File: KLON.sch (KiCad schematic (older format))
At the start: 37 parts

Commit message: organization. Fixed Values. Stage 1 is complete.
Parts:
- C?: value 3.2n -> 2.2n
- RV?: value POT -> GAIN2
- RV?: value POT -> GAIN1
- gave numbers to parts that had none: 1
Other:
- moved on the sheet: C?, D?, R?, RV?

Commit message: Fixed two connections.
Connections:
- net VB+: now also RV?.2
- net at C?.1, R?.1, R?.2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: now also C?.2
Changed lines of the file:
@@
 LIBS:contrib
 LIBS:valves
-LIBS:dk_USB-DVI-HDMI-Connectors
-LIBS:dk_TVS-Mixed-Technology
-LIBS:dk_TVS-Diodes
-LIBS:dk_Trimmer-Potentiometers
-LIBS:dk_Transistors-JFETs
-LIBS:dk_Transistors-FETs-MOSFETs-Single
-LIBS:dk_Transistors-FETs-MOSFETs-RF
-LIBS:dk_Transistors-FETs-MOSFETs-Arrays
-LIBS:dk_Transistors-Bipolar-BJT-Single
-LIBS:dk_Transistors-Bipolar-BJT-Single-Pre-Biased
-LIBS:dk_Transistors-Bipolar-BJT-RF
-LIBS:dk_Transistors-Bipolar-BJT-Arrays
-LIBS:dk_Toggle-Switches
-LIBS:dk_Thyristors-TRIACs
-LIBS:dk_Thyristors-SCRs
-LIBS:dk_Thyristors-DIACs-SIDACs
-LIBS:dk_Thermal-Cutoffs-Thermal-Fuses
-LIBS:dk_Temperature-Sensors-Analog-and-Digital-Output
-LIBS:dk_Tactile-Switches
-LIBS:dk_Surge-Suppression-ICs
-LIBS:dk_Specialized-Sensors
-LIBS:dk_Specialized-ICs
-LIBS:dk_Solid-State-Relays
-LIBS:dk_Slide-Switches
-LIBS:dk_Signal-Relays-Up-to-2-Amps
-LIBS:dk_Sensors-Transducers_Accessories
-LIBS:dk_Rotary-Potentiometers-Rheostats
-LIBS:dk_RFID-RF-Access-Monitoring-ICs
-LIBS:dk_RF-Transmitters
-LIBS:dk_RF-Transceiver-Modules
-LIBS:dk_RF-Transceiver-ICs
-LIBS:dk_RF-Switches
-LIBS:dk_RF-Receivers
-LIBS:dk_RF-Evaluation-and-Development-Kits-Boards
-LIBS:dk_RF-Detectors
-LIBS:dk_RF-Demodulators
-LIBS:dk_RF-Antennas
-LIBS:dk_RF-Amplifiers
-LIBS:dk_Resistor-Networks-Arrays
-LIBS:dk_Reed-Relays
-LIBS:dk_Rectangular-Connectors-Headers-Male-Pins
-LIBS:dk_Pushbutton-Switches
-LIBS:dk_Programmable-Oscillators
-LIBS:dk_Pressure-Sensors-Transducers
-LIBS:dk_Power-Relays-Over-2-Amps
-LIBS:dk_PMIC-Voltage-Regulators-Special-Purpose
-LIBS:dk_PMIC-Voltage-Regulators-Linear
-LIBS:dk_PMIC-Voltage-Regulators-DC-DC-Switching-Regulators
-LIBS:dk_PMIC-Voltage-Regulators-DC-DC-Switching-Controllers
-LIBS:dk_PMIC-Voltage-Reference
-LIBS:dk_PMIC-V-F-and-F-V-Converters
-LIBS:dk_PMIC-Thermal-Management
-LIBS:dk_PMIC-Supervisors
-LIBS:dk_PMIC-RMS-to-DC-Converters
-LIBS:dk_PMIC-Power-Management-Specialized
-LIBS:dk_PMIC-Power-Distribution-Switches-Load-Drivers
-LIBS:dk_PMIC-OR-Controllers-Ideal-Diodes
-LIBS:dk_PMIC-Motor-Drivers-Controllers
-LIBS:dk_PMIC-LED-Drivers
-LIBS:dk_PMIC-Gate-Drivers
-LIBS:dk_PMIC-Full-Half-Bridge-Drivers
-LIBS:dk_PMIC-Current-Regulation-Management
-LIBS:dk_PMIC-Battery-Management
-LIBS:dk_PMIC-Battery-Chargers
-LIBS:dk_PMIC-AC-DC-Converters-Offline-Switchers
-LIBS:dk_Oscillators
-LIBS:dk_Optoisolators-Triac-SCR-Output
-LIBS:dk_Optoisolators-Transistor-Photovoltaic-Output
-LIBS:dk_Optoisolators-Logic-Output
-LIBS:dk_Optical-Sensors-Reflective-Analog-Output
-LIBS:dk_Optical-Sensors-Phototransistors
-LIBS:dk_Optical-Sensors-Photodiodes
-LIBS:dk_Optical-Sensors-Photo-Detectors-Remote-Receiver
-LIBS:dk_Optical-Sensors-Ambient-Light-IR-UV-Sensors
-LIBS:dk_Navigation-Switches-Joystick
-LIBS:dk_Motion-Sensors-Tilt-Switches
-LIBS:dk_Motion-Sensors-IMUs-Inertial-Measurement-Units
-LIBS:dk_Motion-Sensors-Accelerometers
-LIBS:dk_Modular-Connectors-Jacks
-LIBS:dk_Modular-Connectors-Jacks-With-Magnetics
-LIBS:dk_Microphones
-LIBS:dk_Memory
-LIBS:dk_Memory-Connectors-PC-Card-Sockets
-LIBS:dk_Magnetic-Sensors-Switches-Solid-State
-LIBS:dk_Magnetic-Sensors-Linear-Compass-ICs
-LIBS:dk_Magnetic-Sensors-Compass-Magnetic-Field-Modules
-LIBS:dk_Logic-Translators-Level-Shifters
-LIBS:dk_Logic-Signal-Switches-Multiplexers-Decoders
-LIBS:dk_Logic-Shift-Registers
-LIBS:dk_Logic-Multivibrators
-LIBS:dk_Logic-Gates-and-Inverters
-LIBS:dk_Logic-Flip-Flops
-LIBS:dk_Logic-Buffers-Drivers-Receivers-Transceivers
-LIBS:dk_Linear-Comparators
-LIBS:dk_Linear-Amplifiers-Instrumentation-OP-Amps-Buffer-Amps
-LIBS:dk_Linear-Amplifiers-Audio
-LIBS:dk_LEDs-Circuit-Board-Indicators-Arrays-Light-Bars-Bar-Graphs
-LIBS:dk_LED-Indication-Discrete
-LIBS:dk_Interface-Specialized
-LIBS:dk_Interface-Sensor-Capacitive-Touch
-LIBS:dk_Interface-Sensor-and-Detector-Interfaces
-LIBS:dk_Interface-Modules
-LIBS:dk_Interface-I-O-Expanders
-LIBS:dk_Interface-Drivers-Receivers-Transceivers
-LIBS:dk_Interface-Controllers
-LIBS:dk_Interface-Analog-Switches-Special-Purpose
-LIBS:dk_Interface-Analog-Switches-Multiplexers-Demultiplexers
-LIBS:dk_Inrush-Current-Limiters-ICL
-LIBS:dk_Infrared-UV-Visible-Emitters
-LIBS:dk_Image-Sensors-Camera
-LIBS:dk_Humidity-Moisture-Sensors
-LIBS:dk_Gas-Sensors
-LIBS:dk_Fuses
-LIBS:dk_Fixed-Inductors
-LIBS:dk_Ferrite-Beads-and-Chips
-LIBS:dk_Evaluation-Boards-Sensors
-LIBS:dk_Encoders
-LIBS:dk_Embedded-Microcontrollers
-LIBS:dk_Display-Modules-LED-Character-and-Numeric
-LIBS:dk_Diodes-Zener-Single
-LIBS:dk_Diodes-Rectifiers-Single
-LIBS:dk_Diodes-Rectifiers-Arrays
-LIBS:dk_Diodes-Bridge-Rectifiers
-LIBS:dk_Digital-Isolators
-LIBS:dk_DC-DC-Converters
-LIBS:dk_Data-Acquisition-Touch-Screen-Controllers
-LIBS:dk_Data-Acquisition-Digital-to-Analog-Converters-DAC
-LIBS:dk_Data-Acquisition-Digital-Potentiometers
-LIBS:dk_Data-Acquisition-Analog-to-Digital-Converters-ADC
-LIBS:dk_Data-Acquisition-ADCs-DACs-Special-Purpose
-LIBS:dk_D-Sub-Connectors
-LIBS:dk_Current-Transducers
-LIBS:dk_Coaxial-Connectors-RF
-LIBS:dk_Clock-Timing-Real-Time-Clocks
-LIBS:dk_Clock-Timing-Programmable-Timers-and-Oscillators
-LIBS:dk_Clock-Timing-Clock-Generators-PLLs-Frequency-Synthesizers
-LIBS:dk_Battery-Holders-Clips-Contacts
-LIBS:dk_Barrel-Audio-Connectors
-LIBS:dk_Balun
-LIBS:dk_Automotive-Relays
-LIBS:dk_Alarms-Buzzers-and-Sirens
-LIBS:dk_Addressable-Specialty
 LIBS:3PDT
 LIBS:KLON-cache
@@
 	3050 3900 3000 3900
 Wire Wire Line
-	3000 3650 3050 3650
+	3050 3650 3000 3650
 Connection ~ 3050 3650
 Wire Wire Line
@@
 Connection ~ 3050 3150
 Wire Wire Line
-	3150 3400 3050 3400
+	3050 3400 3150 3400
 Connection ~ 3050 3400
 Wire Wire Line
@@
 Connection ~ 2650 3650
 Wire Wire Line
-	3450 3400 3700 3400
+	3700 3400 3450 3400
 Wire Wire Line
 	3450 3150 3700 3150
@@
 	3650 2650 3800 2650
 Wire Wire Line
-	3700 3400 3700 2650
+	3700 2650 3700 3400
 Connection ~ 3700 2650
 Connection ~ 3700 3150
@@
 	5500 3500 5500 4100
 Connection ~ 5500 4100
+Text GLabel 2425 2950 0    60   Input ~ 0
+VB+
+Wire Wire Line
+	2425 2950 2500 2950
+Wire Wire Line
+	1700 3450 1700 3500
+Wire Wire Line
+	1700 3500 1450 3500
+Connection ~ 1450 3500
 $EndSCHEMATC

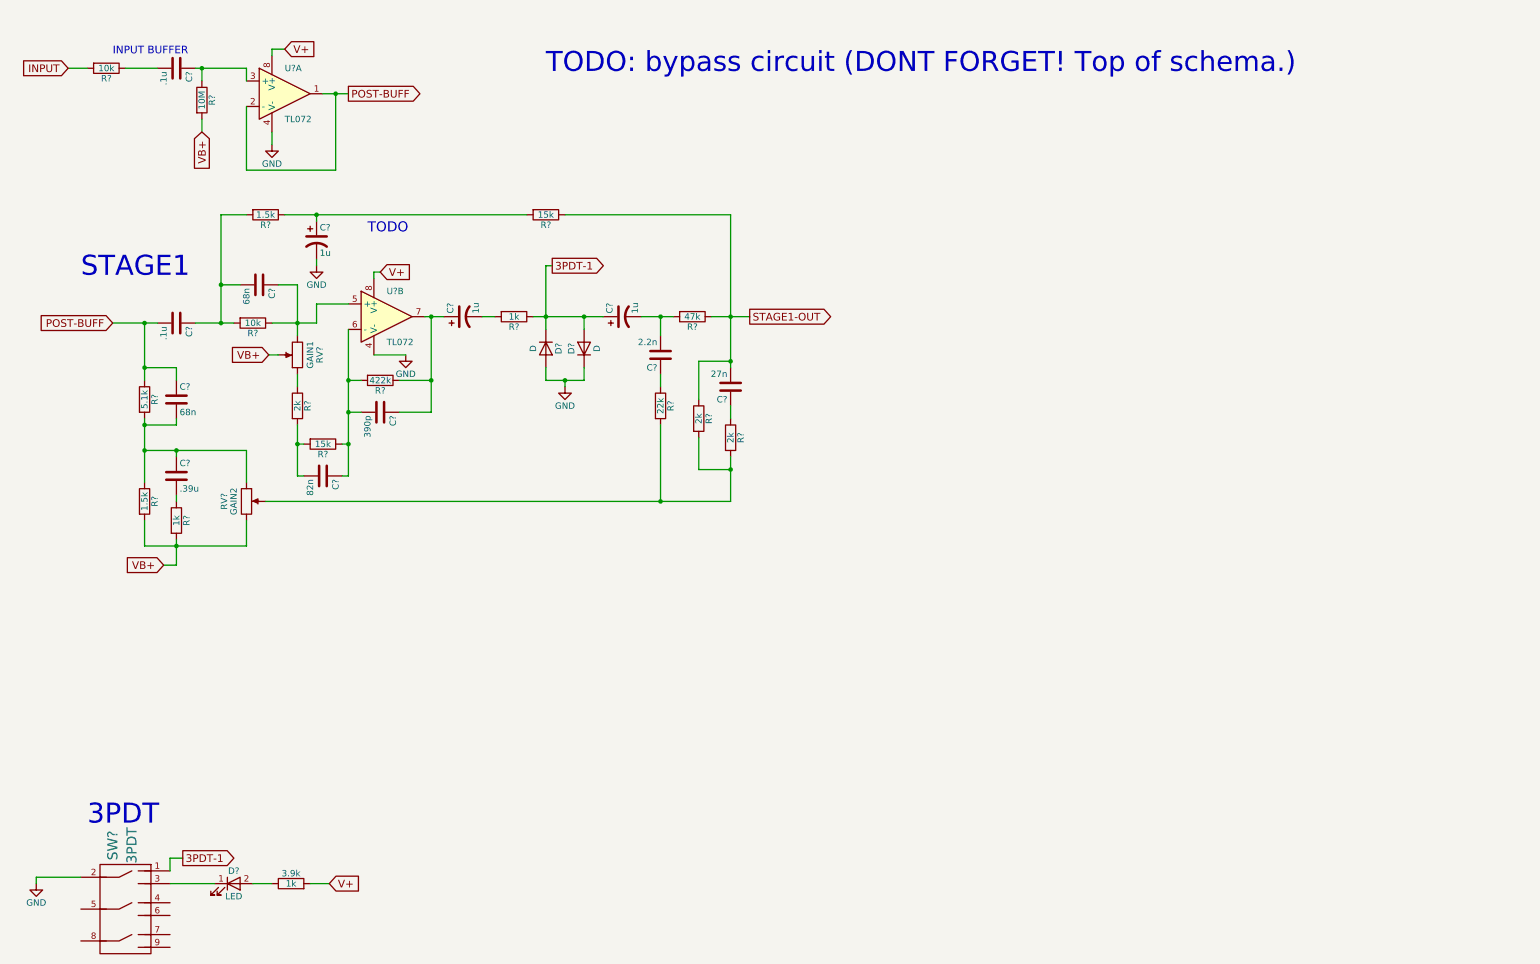
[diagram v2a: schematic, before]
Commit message: Finished schematic. Needs to be double checked. Added a couple of libs and footprints.
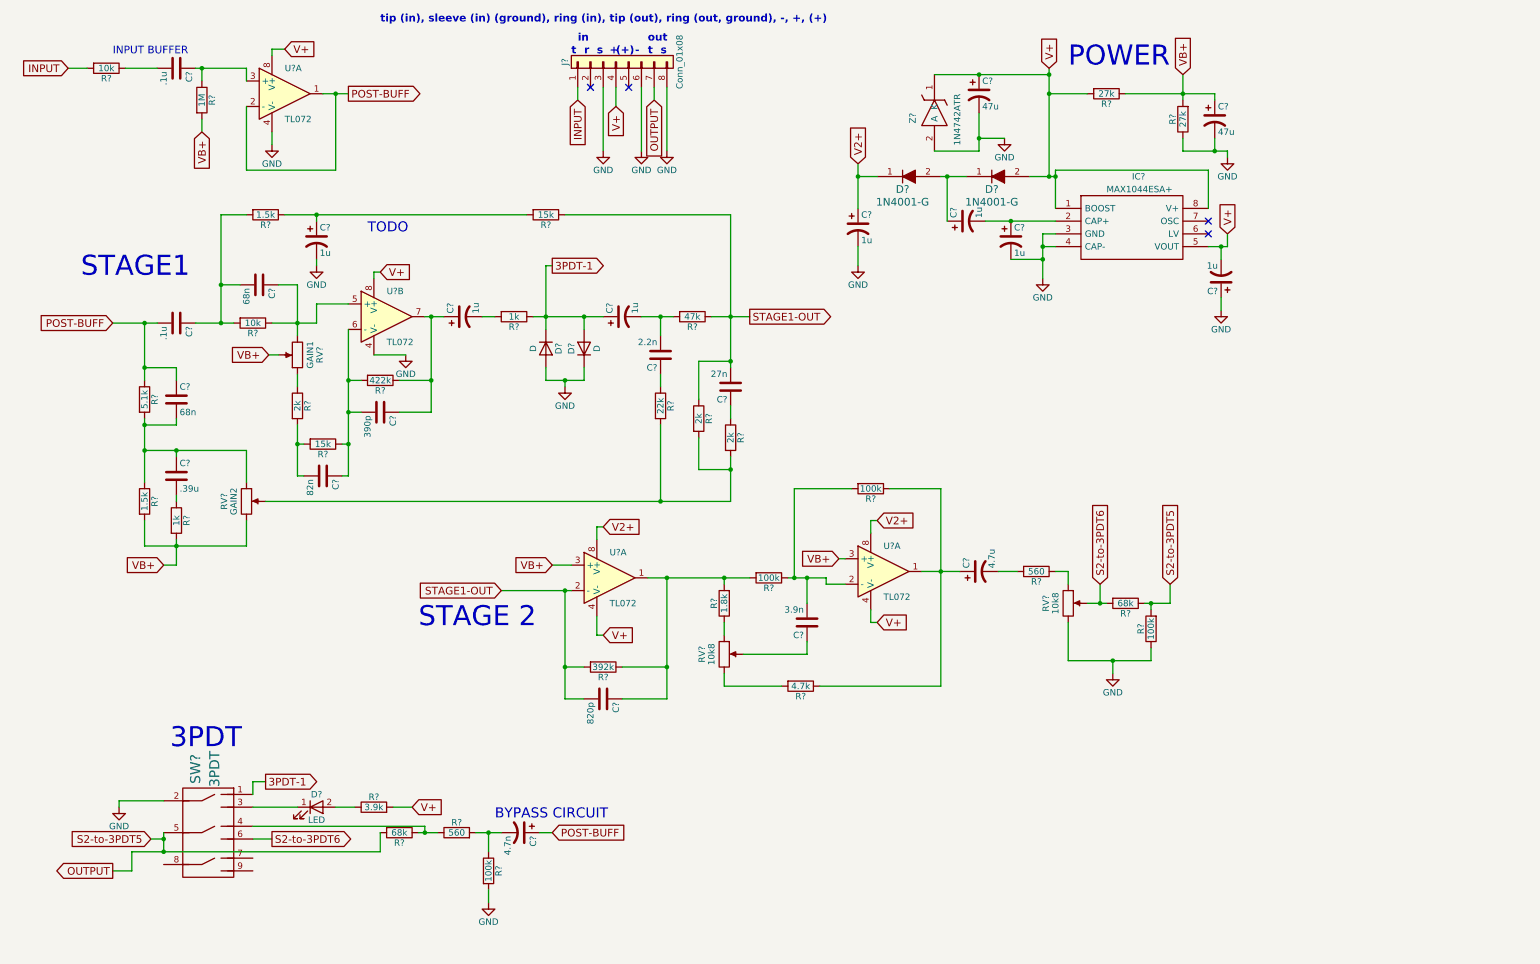
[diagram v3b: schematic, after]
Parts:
- added C?: 820p, symbol C
- added C?: 3.9n, symbol C
- added C?: 4.7u, symbol CP1
- added C?: 4.7n, symbol CP1
- added C? (x4): 1u, symbol CP1
- added C? (x2): 47u, symbol CP1
- added D? (x2): 1N4001-G, digikey-footprints:DO-41, symbol 1N4001-G
- added IC?: MAX1044ESA+, SOIC127P600X175-8N, symbol MAX1044ESA+
- added J?: Conn_01x08, symbol Conn_01x08
- added R?: 392k, symbol R
- added R?: 1.8k, symbol R
- added R? (x4): 100k, symbol R
- added R?: 4.7k, symbol R
- added R? (x2): 560, symbol R
- added R? (x2): 68k, symbol R
- added R? (x2): 27k, symbol R
- added RV? (x2): 10k8, symbol POT
- added U? (x2): TL072, symbol TL072
- added Z?: 1N4742ATR, DIOAD1413W86L463D238, symbol 1N4742ATR
- R?: value 10M -> 1M
- R?: renamed from 3.9k; value 1k -> 3.9k
- RV? (x2): Note (none) -> DUAL POT
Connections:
- net GND: now also C?.1, C?.2, C?.2, C?.2, C?.2, IC?.3 (GND), IC?.4 (CAP-), J?.3 (Pin_3), J?.6 (Pin_6), J?.8 (Pin_8), R?.1, R?.1, R?.2, RV?.3, Z?.2 (A)
- net INPUT: now also J?.1 (Pin_1)
- net POST-BUFF: now also C?.1
- net STAGE1-OUT: now also C?.2, R?.2, U?.2 (-)
- net V+: now also C?.1, C?.2, D?.2, IC?.1 (BOOST), IC?.5 (VOUT), IC?.8 (V+), J?.4 (Pin_4), R?.2, U?.4 (V-), U?.4 (V-), Z?.1 (K)
- net VB+: now also C?.1, R?.1, R?.2, U?.3 (+), U?.3 (+)
- net at SW?.4: now also R?.1, R?.1
- net OUTPUT: now reaches SW?.5
- net OUTPUT: now also J?.7 (Pin_7), R?.1, R?.2, R?.2
- net S2-to-3PDT6: now reaches SW?.6
- net S2-to-3PDT6: now also R?.2, RV?.2
- new net: C?.1, R?.1, R?.2, R?.2, U?.1
- new net: R?.1, RV?.1 (x2)
- new net: C?.2, R?.1, R?.2, U?.2 (-)
- new net: C?.1, RV?.2
- new net: R?.2, RV?.3
- new net: C?.1, R?.1, R?.1, U?.1
- new net: C?.2, R?.2
- new net: C?.2, R?.1, R?.2
- new net: C?.1, C?.2, IC?.2 (CAP+)
- new net: C?.1, D?.1, D?.2
- new net V2+: C?.1, D?.1, U?.8 (V+), U?.8 (V+)
- no-connect marks 0 -> 4
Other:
- note added: "(+)"
- note added: "+"
- note added: "-"
- note added: "BYPASS CIRCUIT"
- note added: "POWER"
- note added: "STAGE 2"
- note added: "in"
- note added: "out"
- note added: "r"
- note added: "s"
- note added: "t"
- note added: "tip (in), sleeve (in) (ground), ring (in), tip (out), ring (out, ground), -, +, (+)"
- note removed: "TODO: bypass circuit (DONT FORGET! Top of schema.)"
- moved on the sheet: D?, R?, SW?

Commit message: Changed connectors for in, out, power. Added footprints for several parts. Correlated footprints to parts. Started PCB.
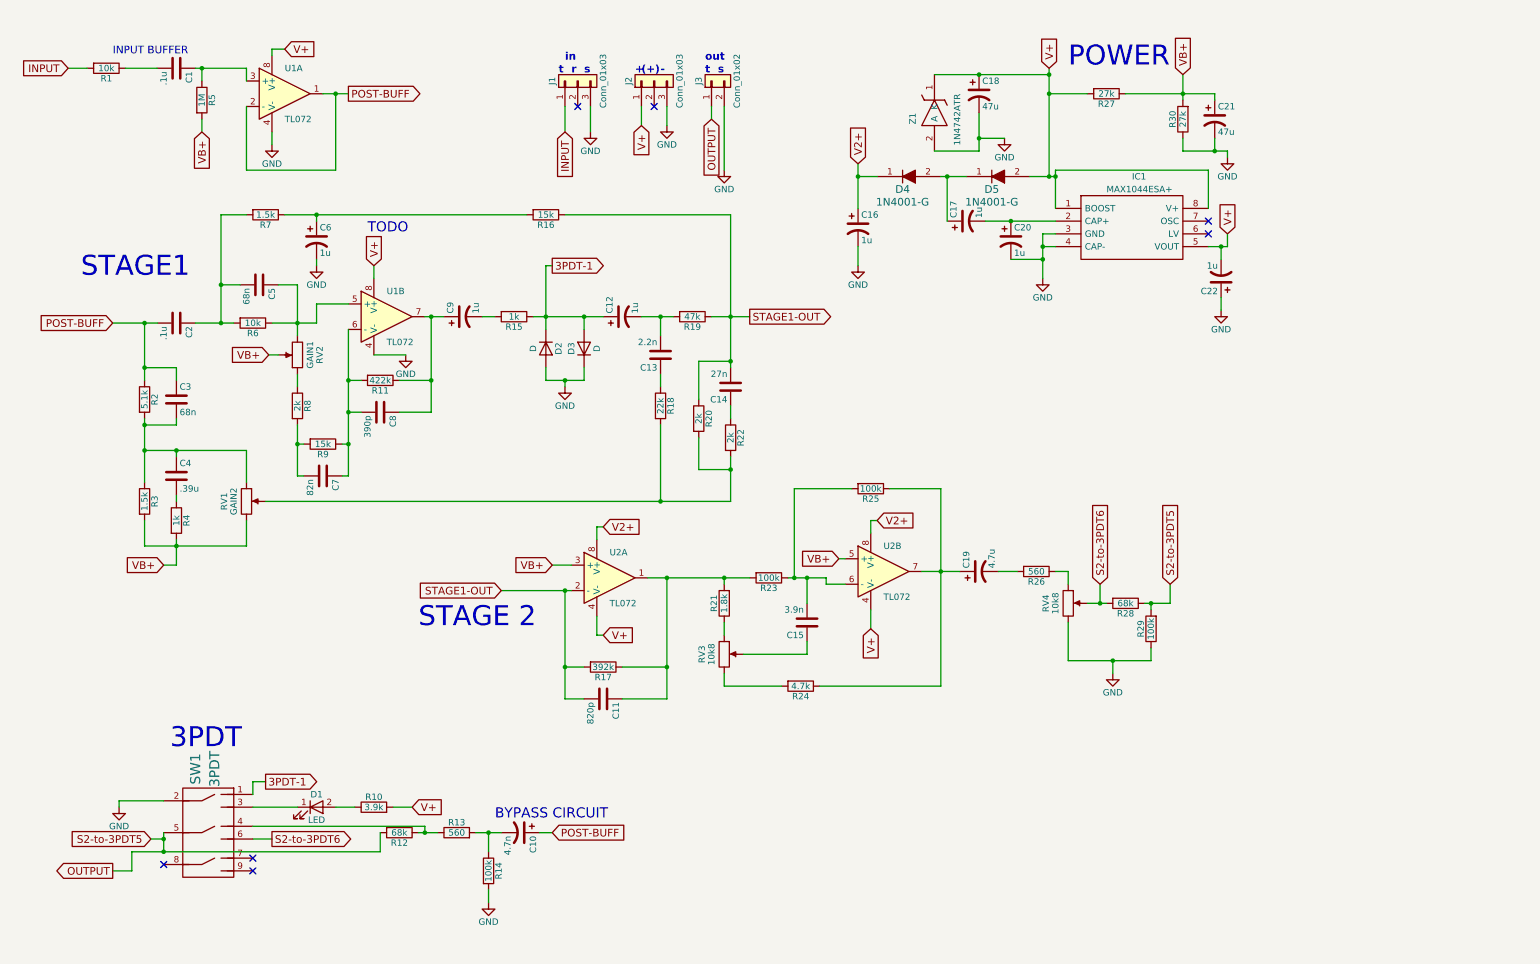
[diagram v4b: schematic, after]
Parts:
- removed J?: Conn_01x08, symbol Conn_01x08
- added J1, J2: Conn_01x03, Socket_Strips:Socket_Strip_Straight_1x03_Pitch2.54mm, symbol Conn_01x03
- added J3: Conn_01x02, Socket_Strips:Socket_Strip_Straight_1x02_Pitch2.54mm, symbol Conn_01x02
- C1, C11, C2, C3, C4, C5, C8: renamed from C?; footprint (none) -> Capacitors_THT:C_Rect_L7.0mm_W2.5mm_P5.00mm
- C10, C13, C14, C15, C7: renamed from C?; footprint (none) -> Capacitors_THT:C_Rect_L7.0mm_W2.0mm_P5.00mm
- C12, C16, C17, C18, C19, C20, C21, C22, C6, C9: renamed from C?; footprint (none) -> Capacitors_THT:CP_Radial_D5.0mm_P2.00mm
- D1: renamed from D?; footprint (none) -> LEDs:LED_D1.8mm_W3.3mm_H2.4mm
- D2, D3: renamed from D?; footprint (none) -> Diodes_THT:D_A-405_P7.62mm_Horizontal
- R1, R10, R11, R12, R13, R14, R15, R16, R17, R18, R19, R2, R20, R21, R22, R23, R24, R25, R26, R27, R28, R29, R3, R30, R4, R5, R6, R7, R8, R9: renamed from R?; footprint (none) -> Resistors_THT:R_Axial_DIN0207_L6.3mm_D2.5mm_P10.16mm_Horizontal
- RV1, RV2, RV3, RV4: renamed from RV?; footprint (none) -> Potentiometers:Potentiometer_WirePads_Small
- SW1: renamed from SW?; footprint (none) -> projectfootprints:3PDT
- U1, U2: renamed from U?; footprint (none) -> Housings_DIP:DIP-8_W7.62mm
- gave numbers to parts that had none: 4
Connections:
- net GND: now also J1.3 (Pin_3), J2.3 (Pin_3), J3.2 (Pin_2)
- net INPUT: now also J1.1 (Pin_1)
- net OUTPUT: now also J3.1 (Pin_1)
- net V+: now also J2.1 (Pin_1)
- net VB+: now also U2.5 (+); no longer U2.3 (+)
- net at C15.2, R23.1, R25.2: now also U2.6 (-); no longer U2.2 (-)
- net at C19.1, R24.1, R25.1: now also U2.7; no longer U2.1
- no-connect marks 4 -> 7
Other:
- note removed: "tip (in), sleeve (in) (ground), ring (in), tip (out), ring (out, ground), -, +, (+)"
